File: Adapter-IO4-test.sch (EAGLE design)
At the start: 22 parts, among them CON1 CONNECTOR-IO4INV

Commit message: simplified design
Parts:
- removed LED5, LED6, LED7, LED8: (no value), SPCoast:LEDLED5MM
- added BOARD1: BOARD50X50-NOHOLES, SPCoast:BOARD50X50-NOHOLES
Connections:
- net GND: no longer LED5.C, LED6.C, LED7.C, LED8.C
- net N$16: no longer LED8.A
- net N$2: no longer LED5.A
- net N$4: no longer LED6.A
- net N$6: no longer LED7.A
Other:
- note added: "IO4 test board"
- note removed: "A Template for Eagle Projects"

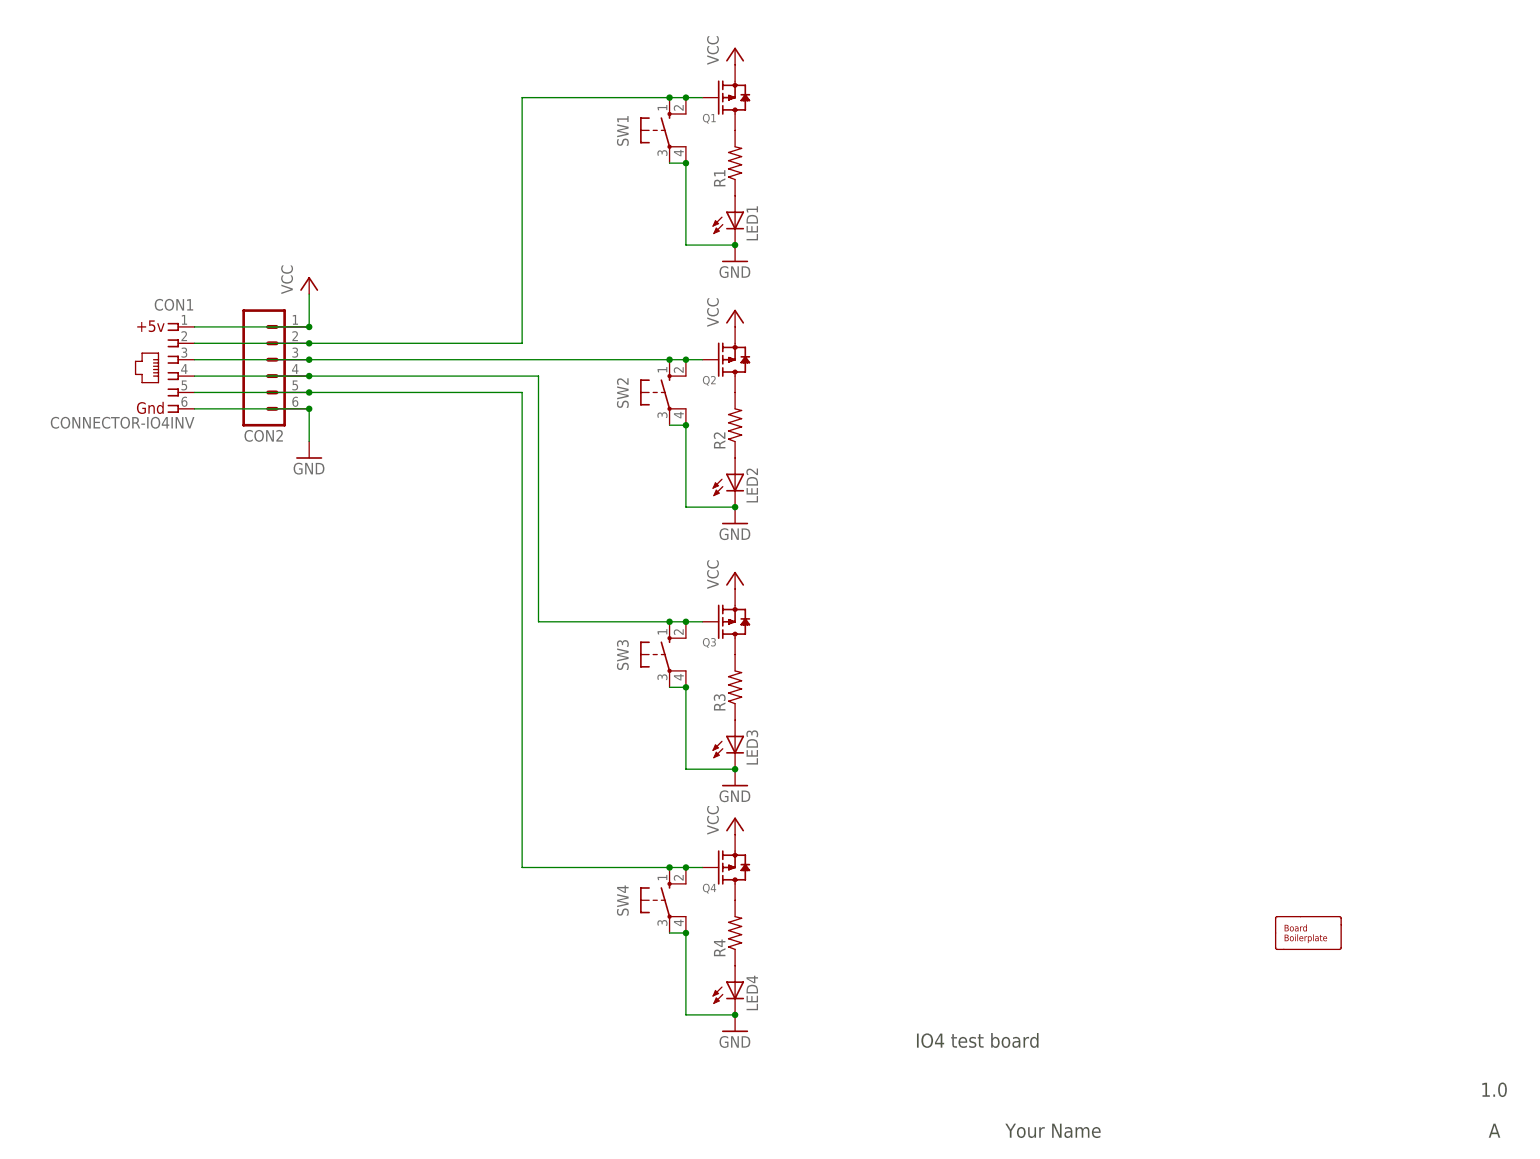
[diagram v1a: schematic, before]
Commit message: added values to schematic
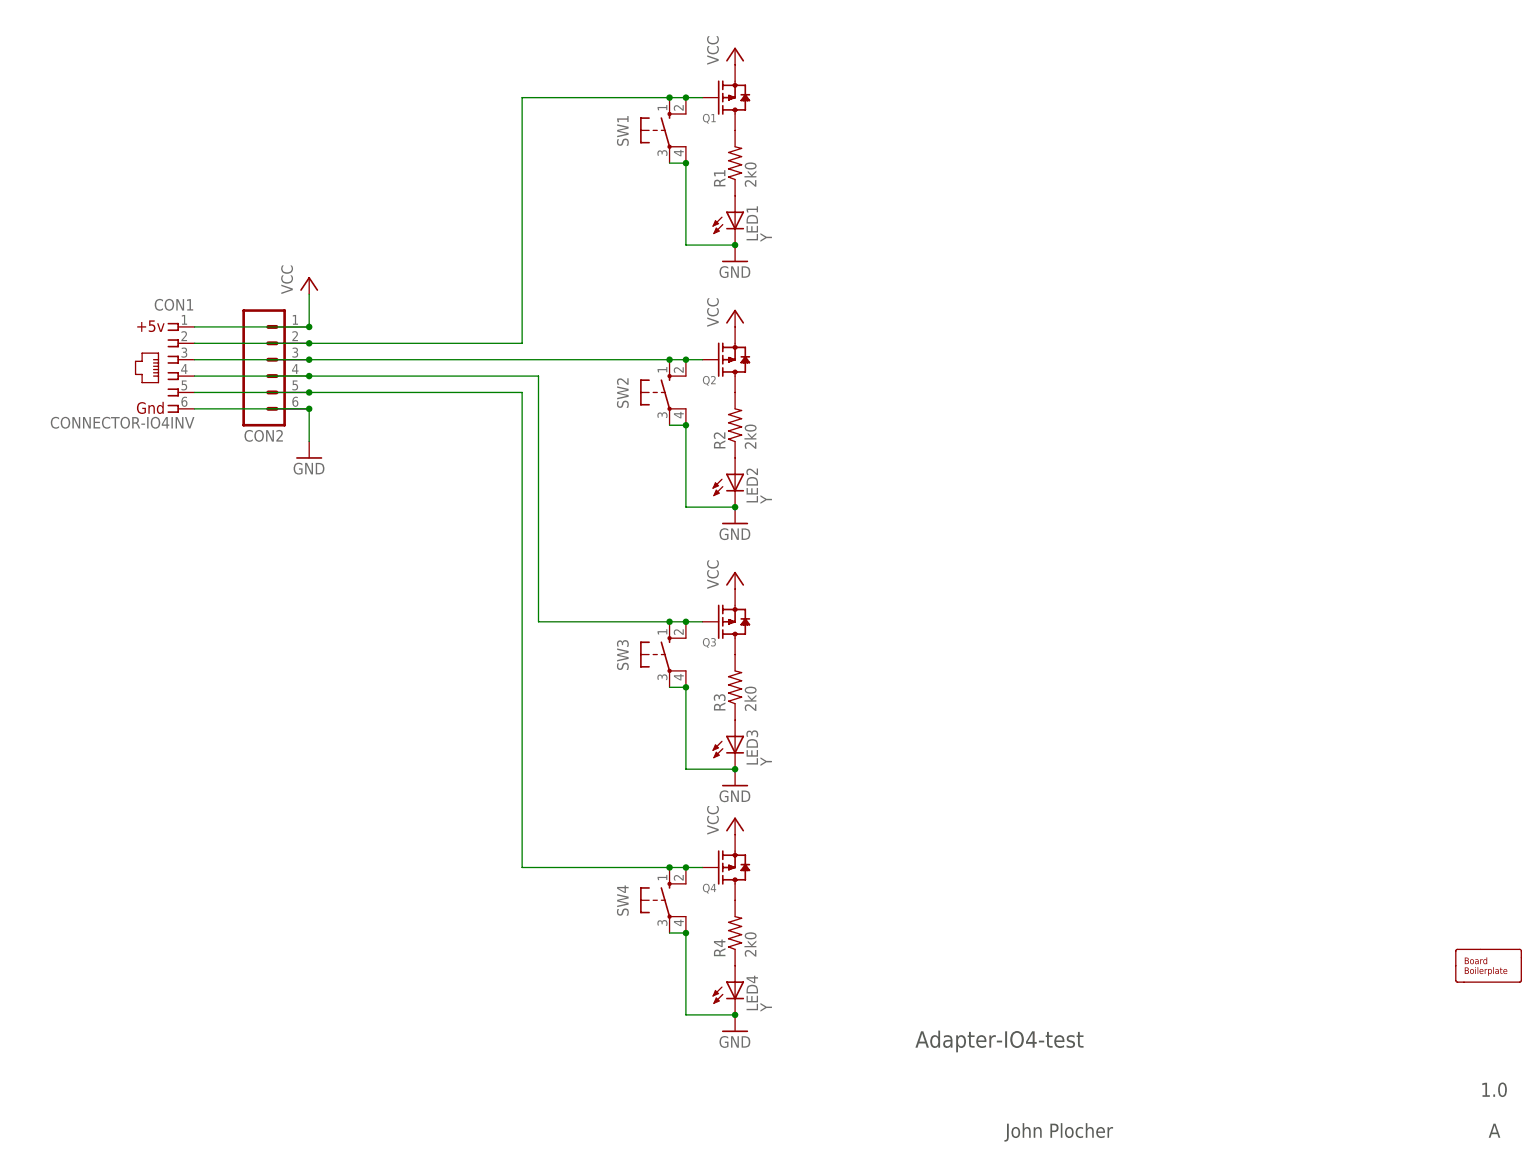
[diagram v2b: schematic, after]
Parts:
- LED1, LED2, LED3, LED4: value (none) -> Y
- R1, R2, R3, R4: value (none) -> 2k0
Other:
- note added: "John Plocher"
- note removed: "IO4 test board"
- note removed: "Your Name"
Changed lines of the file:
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@@
 <layer number="93" name="Pins" color="2" fill="1" visible="no" active="yes"/>
 <layer number="94" name="Symbols" color="4" fill="1" visible="yes" active="yes"/>
-<layer number="95" name="Names" color="7" fill="1" visible="yes" active="yes"/>
-<layer number="96" name="Values" color="7" fill="1" visible="yes" active="yes"/>
-<layer number="97" name="Info" color="7" fill="1" visible="yes" active="yes"/>
+<layer number="95" name="Names" color="19" fill="1" visible="yes" active="yes"/>
+<layer number="96" name="Values" color="39" fill="1" visible="yes" active="yes"/>
+<layer number="97" name="Info" color="39" fill="1" visible="yes" active="yes"/>
 <layer number="98" name="Guide" color="6" fill="1" visible="yes" active="yes"/>
 <layer number="99" name="Anatomie" color="7" fill="1" visible="yes" active="yes"/>
@@
 <part name="P+1" library="SPCoast" deviceset="VCC" device=""/>
 <part name="GND1" library="SPCoast" deviceset="GND" device=""/>
-<part name="LED1" library="SPCoast" deviceset="LED*" device="0805-LED"/>
-<part name="LED2" library="SPCoast" deviceset="LED*" device="0805-LED"/>
-<part name="LED3" library="SPCoast" deviceset="LED*" device="0805-LED"/>
-<part name="LED4" library="SPCoast" deviceset="LED*" device="0805-LED"/>
-<part name="R1" library="SPCoast" deviceset="R*" device="0805-RES"/>
-<part name="R2" library="SPCoast" deviceset="R*" device="0805-RES"/>
-<part name="R3" library="SPCoast" deviceset="R*" device="0805-RES"/>
-<part name="R4" library="SPCoast" deviceset="R*" device="0805-RES"/>
+<part name="LED1" library="SPCoast" deviceset="LED*" device="0805-LED" value="Y"/>
+<part name="LED2" library="SPCoast" deviceset="LED*" device="0805-LED" value="Y"/>
+<part name="LED3" library="SPCoast" deviceset="LED*" device="0805-LED" value="Y"/>
+<part name="LED4" library="SPCoast" deviceset="LED*" device="0805-LED" value="Y"/>
+<part name="R1" library="SPCoast" deviceset="R*" device="0805-RES" value="2k0"/>
+<part name="R2" library="SPCoast" deviceset="R*" device="0805-RES" value="2k0"/>
+<part name="R3" library="SPCoast" deviceset="R*" device="0805-RES" value="2k0"/>
+<part name="R4" library="SPCoast" deviceset="R*" device="0805-RES" value="2k0"/>
 <part name="P+2" library="SPCoast" deviceset="VCC" device=""/>
 <part name="GND2" library="SPCoast" deviceset="GND" device=""/>
@@
 <sheet>
 <plain>
-<text x="152.4" y="20.32" size="2.1844" layer="97">IO4 test board</text>
+<text x="152.4" y="20.32" size="2.54" layer="97" ratio="10">&gt;DRAWING_NAME</text>
 <text x="240.03" y="12.7" size="2.1844" layer="97">1.0</text>
 <text x="241.3" y="6.35" size="2.1844" layer="97">A</text>
-<text x="166.37" y="6.35" size="2.1844" layer="97">Your Name</text>
+<text x="166.37" y="6.35" size="2.1844" layer="97">John Plocher</text>
 </plain>
 <instances>
@@
 <instance part="P+4" gate="VCC" x="124.46" y="93.98"/>
 <instance part="P+5" gate="VCC" x="124.46" y="55.88"/>
-<instance part="BOARD1" gate="B" x="213.36" y="38.1"/>
+<instance part="BOARD1" gate="B" x="241.3" y="33.02"/>
 </instances>
 <busses>

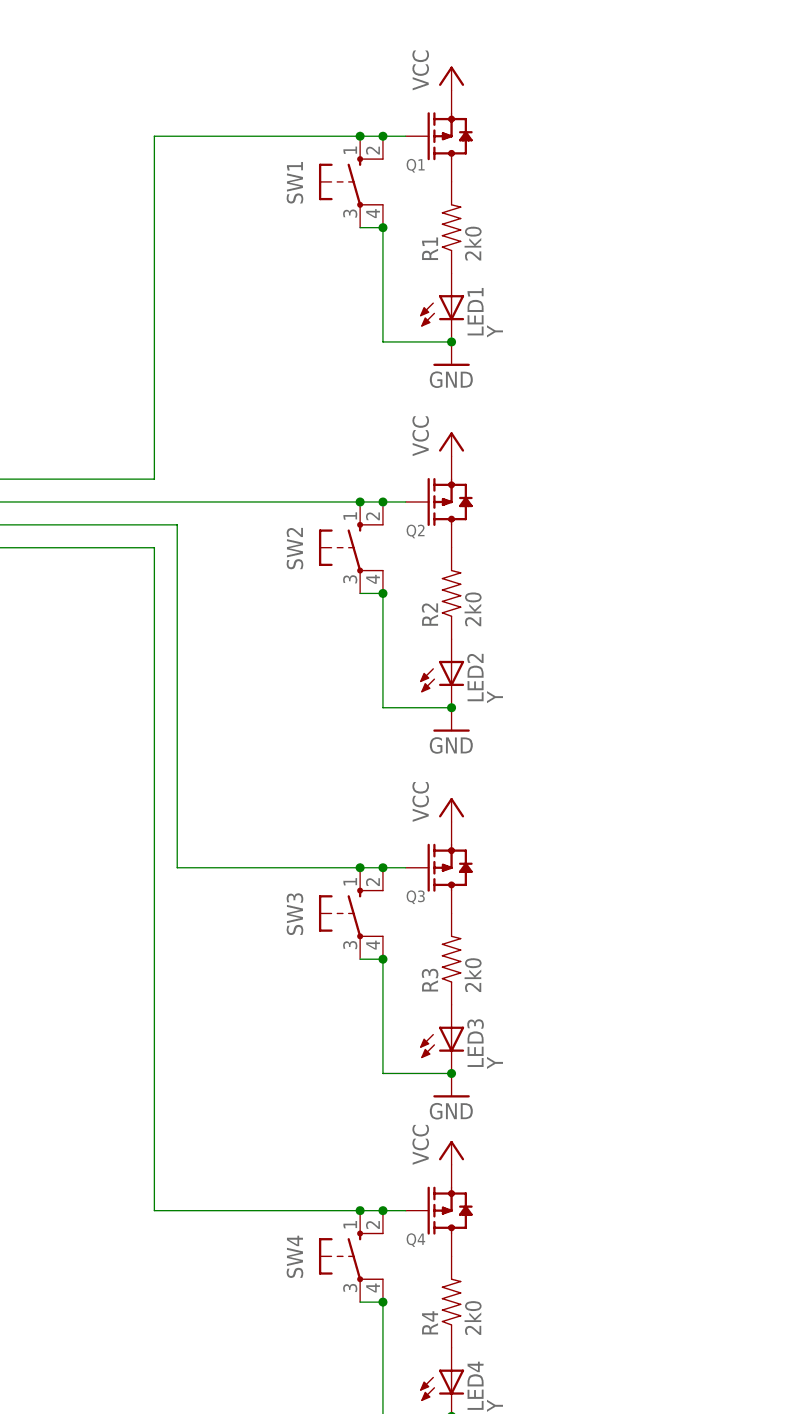
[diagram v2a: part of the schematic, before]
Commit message: added values to schematic
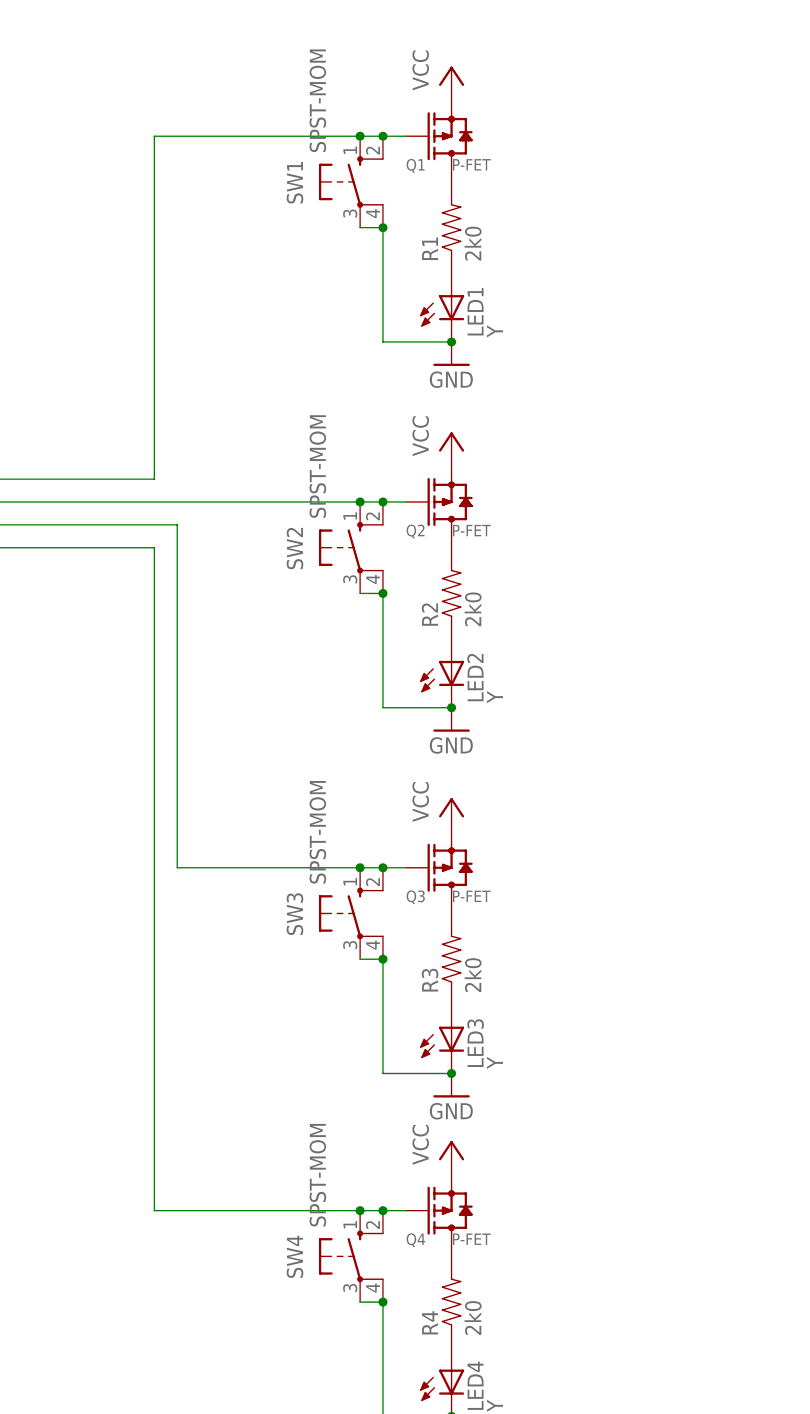
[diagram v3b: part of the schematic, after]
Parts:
- Q1, Q2, Q3, Q4: value (none) -> P-FET
- SW1, SW2, SW3, SW4: value (none) -> SPST-MOM
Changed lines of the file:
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@@
 <part name="CON1" library="SPCoast" deviceset="CONNECTOR-IO4" device="INV"/>
 <part name="CON2" library="SPCoast" deviceset="CONNECTOR-M06" device="LOCK"/>
-<part name="Q1" library="SPCoast" deviceset="MOSFET-P" device=""/>
-<part name="Q2" library="SPCoast" deviceset="MOSFET-P" device=""/>
-<part name="Q3" library="SPCoast" deviceset="MOSFET-P" device=""/>
-<part name="Q4" library="SPCoast" deviceset="MOSFET-P" device=""/>
-<part name="SW1" library="SPCoast" deviceset="SWITCH-10-XX" device=""/>
-<part name="SW2" library="SPCoast" deviceset="SWITCH-10-XX" device=""/>
-<part name="SW3" library="SPCoast" deviceset="SWITCH-10-XX" device=""/>
-<part name="SW4" library="SPCoast" deviceset="SWITCH-10-XX" device=""/>
+<part name="Q1" library="SPCoast" deviceset="MOSFET-P" device="" value="P-FET"/>
+<part name="Q2" library="SPCoast" deviceset="MOSFET-P" device="" value="P-FET"/>
+<part name="Q3" library="SPCoast" deviceset="MOSFET-P" device="" value="P-FET"/>
+<part name="Q4" library="SPCoast" deviceset="MOSFET-P" device="" value="P-FET"/>
+<part name="SW1" library="SPCoast" deviceset="SWITCH-10-XX" device="" value="SPST-MOM"/>
+<part name="SW2" library="SPCoast" deviceset="SWITCH-10-XX" device="" value="SPST-MOM"/>
+<part name="SW3" library="SPCoast" deviceset="SWITCH-10-XX" device="" value="SPST-MOM"/>
+<part name="SW4" library="SPCoast" deviceset="SWITCH-10-XX" device="" value="SPST-MOM"/>
 <part name="P+1" library="SPCoast" deviceset="VCC" device=""/>
 <part name="GND1" library="SPCoast" deviceset="GND" device=""/>

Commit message: bumped sch version
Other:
- note added: "1.1"
- note removed: "1.0"
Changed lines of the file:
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@@
 <plain>
 <text x="152.4" y="20.32" size="2.54" layer="97" ratio="10">&gt;DRAWING_NAME</text>
-<text x="240.03" y="12.7" size="2.1844" layer="97">1.0</text>
+<text x="240.03" y="12.7" size="2.1844" layer="97">1.1</text>
 <text x="241.3" y="6.35" size="2.1844" layer="97">A</text>
 <text x="166.37" y="6.35" size="2.1844" layer="97">John Plocher</text>
